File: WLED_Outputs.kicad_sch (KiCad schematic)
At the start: 52 parts, among them U13 74LV1T126, U14 74LV1T126, U15 74LV1T126, U16 74LV1T126, U17 74LV1T126, U5 TPS2HC08-Q1, U6 74LV1T126

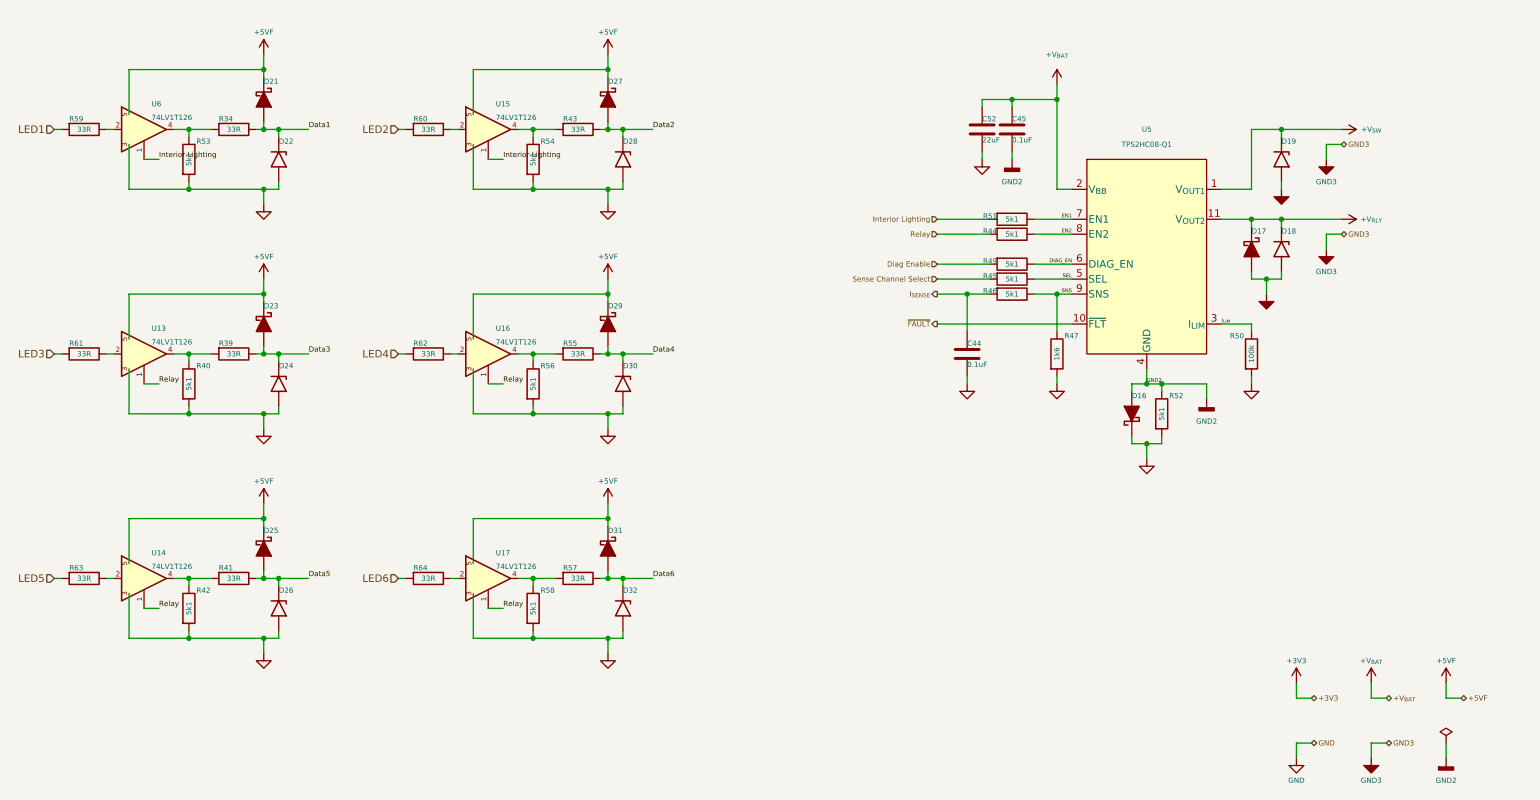
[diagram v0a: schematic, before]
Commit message: Update CANBus_Interface.kicad_sch, ESP32-S3 D1 Pico Board.kicad_sch, ESP32-S3 Pico D1.kicad_pcb, and 15 more files
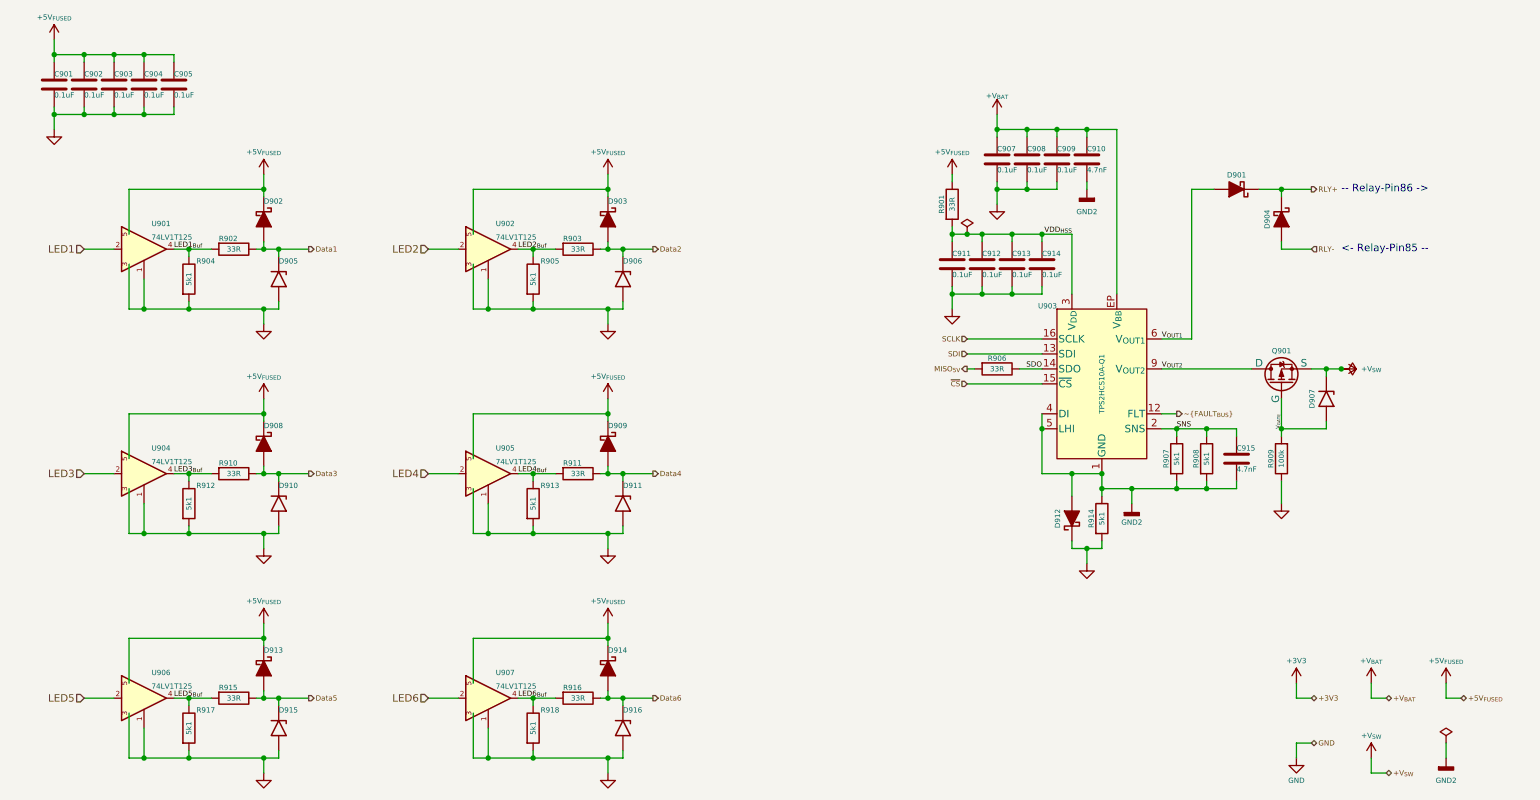
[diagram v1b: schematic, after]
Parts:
- removed C52: 22uF, Capacitors:C_0603_Dense, symbol Device:C
- removed D18: D15V0H1U2LP-7B, Personal_FootprintLibrary:DFN1006-2, symbol PersonalSchematicSymbolLibrary:TVS_Unidirectional
- removed R44, R45, R46, R49, R51: 5k1, Resistors:R_0201_Dense, symbol Device:R
- removed R47: 1k6, Resistors:R_0201_Dense, symbol Device:R
- removed R50: 100k, Resistors:R_0201_Dense, symbol Device:R
- removed R59, R60, R61, R62, R63, R64: 33R, Resistors:R_0201_Dense, symbol Device:R
- removed U13, U14, U15, U16, U6: 74LV1T126, Personal_FootprintLibrary:X2SON5_SOT1226_0.8x0.8mm, symbol 74xxx1Gyy:74LVC1G126
- removed U5: TPS2HC08-Q1, Personal_FootprintLibrary:VQFN-HR-11(C), symbol My Power Management:TPS2HCxx-Q1
- added C901, C902, C903, C904, C905, C907, C908, C909, C911, C912, C913: 0.1uF, My Capacitors:C_0201_Dense, symbol Device:C
- added C910: 4.7nF, My Capacitors:C_0201_Dense, symbol Device:C
- added D904: PMEG4002ESFYL, Personal_FootprintLibrary:DSN0603-2, symbol PersonalSchematicSymbolLibrary:D_Schottky_Filled
- added Q901: NTLJS17D0P03P8Z, My Package_Leadless:WDFN6-4_2.05x2.05mm_P0.65mm, symbol PersonalSchematicSymbolLibrary:NTLJS17D0P03P8Z
- added R901, R906: 33R, My Resistors:R_0201_Dense, symbol Device:R
- added R907, R908: 5k1, My Resistors:R_0201_Dense, symbol Device:R
- added R909: 100k, My Resistors:R_0201_Dense, symbol Device:R
- added U901, U902, U904, U905, U906: 74LV1T125, Personal_FootprintLibrary:X2SON5_SOT1226_0.8x0.8mm, symbol 74xxx1Gyy:74LVC1G125
- added U903: TPS2HCS10A-Q1, My Package_SO:Texas_HTSSOP-16-1EP_5.0x4.4mm_P0.65mm_EP5.0x3.4mm_Mask3.313x2.78mm, symbol My Power Management:TPS2HCSxx-Q1
- C914: renamed from C45; footprint Capacitors:C_0201_Dense -> My Capacitors:C_0201_Dense
- C915: renamed from C44; value 0.1uF -> 4.7nF; footprint Capacitors:C_0201_Dense -> My Capacitors:C_0201_Dense; Distributor Link 1 https://www.digikey.com/en/products/detail/murata-electronics/GRT033R61E104KE01D/10696558 -> https://www.digikey.com/en/products/detail/murata-electronics/GRM033R71E472KE14D/6606084; Distributor Link 2 https://www.mouser.com/ProductDetail/Murata-Electronics/GRT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 -> https://www.mouser.com/ProductDetail/Murata-Electronics/GRM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; LCSC C915760 -> C85933; Manufacturer Part Number GRT033R61E104KE01D -> GRM033R71E472KE14D
- D901: renamed from D17; value SDM1100LP-7 -> PMEG4002ESFYL; footprint Personal_FootprintLibrary:DFN2020-2 -> Personal_FootprintLibrary:DSN0603-2; Distributor Link 1 https://www.digikey.com/en/products/detail/diodes-incorpora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 -> https://www.digikey.com/en/products/detail/nexperia-usa-inc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; Distributor Link 2 https://www.mouser.com/ProductDetail/Diodes-Incorporated/SD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 -> https://www.mouser.com/ProductDetail/Nexperia/PMEG4002ESFYL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; LCSC C6999905 -> C22435168; Manufacturer Diodes Incorporated -> Nexperia USA Inc.; Manufacturer Part Number SDM1100LP-7 -> PMEG4002ESFYL
- D902: renamed from D21; value SDM1100LP-7 -> PMEG4002ESFYL; footprint Personal_FootprintLibrary:DFN2020-2 -> Personal_FootprintLibrary:DSN0603-2; Distributor Link 1 https://www.digikey.com/en/products/detail/diodes-incorpora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 -> https://www.digikey.com/en/products/detail/nexperia-usa-inc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; Distributor Link 2 https://www.mouser.com/ProductDetail/Diodes-Incorporated/SD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 -> https://www.mouser.com/ProductDetail/Nexperia/PMEG4002ESFYL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; LCSC C6999905 -> C22435168; Manufacturer Diodes Incorporated -> Nexperia USA Inc.; Manufacturer Part Number SDM1100LP-7 -> PMEG4002ESFYL
- D903: renamed from D27; value SDM1100LP-7 -> PMEG4002ESFYL; footprint Personal_FootprintLibrary:DFN2020-2 -> Personal_FootprintLibrary:DSN0603-2; Distributor Link 1 https://www.digikey.com/en/products/detail/diodes-incorpora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 -> https://www.digikey.com/en/products/detail/nexperia-usa-inc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; Distributor Link 2 https://www.mouser.com/ProductDetail/Diodes-Incorporated/SD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 -> https://www.mouser.com/ProductDetail/Nexperia/PMEG4002ESFYL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; LCSC C6999905 -> C22435168; Manufacturer Diodes Incorporated -> Nexperia USA Inc.; Manufacturer Part Number SDM1100LP-7 -> PMEG4002ESFYL
- D908: renamed from D23; value SDM1100LP-7 -> PMEG4002ESFYL; footprint Personal_FootprintLibrary:DFN2020-2 -> Personal_FootprintLibrary:DSN0603-2; Distributor Link 1 https://www.digikey.com/en/products/detail/diodes-incorpora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 -> https://www.digikey.com/en/products/detail/nexperia-usa-inc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; Distributor Link 2 https://www.mouser.com/ProductDetail/Diodes-Incorporated/SD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 -> https://www.mouser.com/ProductDetail/Nexperia/PMEG4002ESFYL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; LCSC C6999905 -> C22435168; Manufacturer Diodes Incorporated -> Nexperia USA Inc.; Manufacturer Part Number SDM1100LP-7 -> PMEG4002ESFYL
- D909: renamed from D29; value SDM1100LP-7 -> PMEG4002ESFYL; footprint Personal_FootprintLibrary:DFN2020-2 -> Personal_FootprintLibrary:DSN0603-2; Distributor Link 1 https://www.digikey.com/en/products/detail/diodes-incorpora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 -> https://www.digikey.com/en/products/detail/nexperia-usa-inc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; Distributor Link 2 https://www.mouser.com/ProductDetail/Diodes-Incorporated/SD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 -> https://www.mouser.com/ProductDetail/Nexperia/PMEG4002ESFYL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; LCSC C6999905 -> C22435168; Manufacturer Diodes Incorporated -> Nexperia USA Inc.; Manufacturer Part Number SDM1100LP-7 -> PMEG4002ESFYL
- D912: renamed from D16; value SDM1100LP-7 -> PMEG4002ESFYL; footprint Personal_FootprintLibrary:DFN2020-2 -> Personal_FootprintLibrary:DSN0603-2; Distributor Link 1 https://www.digikey.com/en/products/detail/diodes-incorpora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 -> https://www.digikey.com/en/products/detail/nexperia-usa-inc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; Distributor Link 2 https://www.mouser.com/ProductDetail/Diodes-Incorporated/SD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 -> https://www.mouser.com/ProductDetail/Nexperia/PMEG4002ESFYL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; LCSC C6999905 -> C22435168; Manufacturer Diodes Incorporated -> Nexperia USA Inc.; Manufacturer Part Number SDM1100LP-7 -> PMEG4002ESFYL
- D913: renamed from D25; value SDM1100LP-7 -> PMEG4002ESFYL; footprint Personal_FootprintLibrary:DFN2020-2 -> Personal_FootprintLibrary:DSN0603-2; Distributor Link 1 https://www.digikey.com/en/products/detail/diodes-incorpora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 -> https://www.digikey.com/en/products/detail/nexperia-usa-inc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; Distributor Link 2 https://www.mouser.com/ProductDetail/Diodes-Incorporated/SD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 -> https://www.mouser.com/ProductDetail/Nexperia/PMEG4002ESFYL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; LCSC C6999905 -> C22435168; Manufacturer Diodes Incorporated -> Nexperia USA Inc.; Manufacturer Part Number SDM1100LP-7 -> PMEG4002ESFYL
- D914: renamed from D31; value SDM1100LP-7 -> PMEG4002ESFYL; footprint Personal_FootprintLibrary:DFN2020-2 -> Personal_FootprintLibrary:DSN0603-2; Distributor Link 1 https://www.digikey.com/en/products/detail/diodes-incorpora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 -> https://www.digikey.com/en/products/detail/nexperia-usa-inc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; Distributor Link 2 https://www.mouser.com/ProductDetail/Diodes-Incorporated/SD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 -> https://www.mouser.com/ProductDetail/Nexperia/PMEG4002ESFYL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; LCSC C6999905 -> C22435168; Manufacturer Diodes Incorporated -> Nexperia USA Inc.; Manufacturer Part Number SDM1100LP-7 -> PMEG4002ESFYL
- R902: renamed from R34; footprint Resistors:R_0201_Dense -> My Resistors:R_0201_Dense
- R903: renamed from R43; footprint Resistors:R_0201_Dense -> My Resistors:R_0201_Dense
- R904: renamed from R53; footprint Resistors:R_0201_Dense -> My Resistors:R_0201_Dense
- R905: renamed from R54; footprint Resistors:R_0201_Dense -> My Resistors:R_0201_Dense
- R910: renamed from R39; footprint Resistors:R_0201_Dense -> My Resistors:R_0201_Dense
- R911: renamed from R55; footprint Resistors:R_0201_Dense -> My Resistors:R_0201_Dense
- R912: renamed from R40; footprint Resistors:R_0201_Dense -> My Resistors:R_0201_Dense
- R913: renamed from R56; footprint Resistors:R_0201_Dense -> My Resistors:R_0201_Dense
- R914: renamed from R52; footprint Resistors:R_0201_Dense -> My Resistors:R_0201_Dense
- R915: renamed from R41; footprint Resistors:R_0201_Dense -> My Resistors:R_0201_Dense
- R916: renamed from R57; footprint Resistors:R_0201_Dense -> My Resistors:R_0201_Dense
- R917: renamed from R42; footprint Resistors:R_0201_Dense -> My Resistors:R_0201_Dense
- R918: renamed from R58; footprint Resistors:R_0201_Dense -> My Resistors:R_0201_Dense
- U907: renamed from U17; value 74LV1T126 -> 74LV1T125; symbol 74xxx1Gyy:74LVC1G126 -> 74xxx1Gyy:74LVC1G125; Distributor Link 1 https://www.digikey.com/en/products/detail/nexperia-usa-inc/74LV1T126GXH/8276618 -> https://www.digikey.com/en/products/detail/nexperia-usa-inc/74LV1T125GXH/8276616; Distributor Link 2 https://www.mouser.com/ProductDetail/Nexperia/74LV1T126GXH?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 -> https://www.mouser.com/ProductDetail/Nexperia/74LV1T125GXH?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; LCSC C547942 -> C547939; Manufacturer Part Number 74LV1T126GXH -> 74LV1T125GXH
- renumbered D22 to D905, D28 to D906, D19 to D907, D24 to D910, D30 to D911, D26 to D915, D32 to D916
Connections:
- net I_{SENSE} is gone; now on net SNS: C915.1
- net Relay is gone; now on net GND: U907.1 (OE)
- net +V_{BAT}: now also C907.1, C908.1, C909.1, C910.1, U903.EP (V_{BB}); no longer C914.1
- net +V_{SW}: now also Q901.3 (S), Q901.4 (S)
- net GND: now also C914.2, C901.2, C902.2, C903.2, C904.2, C905.2, C907.2, C908.2, C909.2, C911.2, C912.2, C913.2, R909.1, U901.1 (OE), U901.3 (GND), U902.1 (OE), U902.3 (GND), U904.1 (OE), U904.3 (GND), U905.1 (OE), U905.3 (GND), U906.1 (OE), U906.3 (GND); no longer C915.2
- net GND2: now also C915.2, C910.2, R907.2, R908.2, U903.1 (GND), U903.4 (DI), U903.5 (LHI); no longer C914.2, D901.2 (A)
- net LED1: now also U901.2 (A)
- net LED2: now also U902.2 (A)
- net LED3: now also U904.2 (A)
- net LED4: now also U905.2 (A)
- net LED5: now also U906.2 (A)
- net LED6: now also U907.2 (A)
- net SNS: now also R907.1, R908.1, U903.2 (SNS)
- net LED6_{Buf}: now reaches R916.2, R918.1, U907.4 (Y)
- net LED3_{Buf}: now reaches R910.2, R912.1
- net LED3_{Buf}: now also U904.4 (Y)
- net LED4_{Buf}: now reaches R911.2, R913.1
- net LED4_{Buf}: now also U905.4 (Y)
- net LED5_{Buf}: now reaches R915.2, R917.1
- net LED5_{Buf}: now also U906.4 (Y)
- net LED2_{Buf}: now reaches R903.2, R905.1
- net LED2_{Buf}: now also U902.4 (Y)
- net LED1_{Buf}: now reaches R902.2, R904.1
- net LED1_{Buf}: now also U901.4 (Y)
- net +5VF renamed +5V_{FUSED}
- net +5V_{FUSED}: now also C901.1, C902.1, C903.1, C904.1, C905.1, R901.1, U901.5 (VCC), U902.5 (VCC), U904.5 (VCC), U905.5 (VCC), U906.5 (VCC)
- net +V_{RLY} renamed RLY+
- net RLY+: now also D904.1 (K)
- net GND3 renamed V_{GATE}
- net V_{GATE}: now also Q901.2 (G), R909.2
- new net MISO_{5V}: R906.2
- new net RLY-: D904.2 (A)
- new net SCLK: U903.16 (SCLK)
- new net SDI: U903.13 (SDI)
- new net SDO: R906.1, U903.14 (SDO)
- new net VDD_{HSS}: C911.1, C912.1, C913.1, C914.1, R901.2, U903.3 (V_{DD})
- new net V_{OUT1}: D901.2 (A), U903.6 (V_{OUT1}), U903.7 (V_{OUT1}), U903.8 (V_{OUT1})
- new net V_{OUT2}: Q901.1 (D), U903.10 (V_{OUT2}), U903.11 (V_{OUT2}), U903.9 (V_{OUT2})
- new net ~{CS}: U903.15 (~{CS})
- new net ~{FAULT_{BUS}}: U903.12 (FLT)
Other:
- note added: "-- Relay-Pin86 ->"
- note added: "<- Relay-Pin85 --"
- moved on the sheet: C914, C915, D901, D902, D903, D905, D906, D907, D908, D909, D910, D911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
